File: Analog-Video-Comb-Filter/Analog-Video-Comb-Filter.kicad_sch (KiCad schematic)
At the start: 97 parts, among them J1 12VDC(+), J2 SVHS, J3 CVBS, Q1 BC548, Q10 BC548, Q2 BC548, Q3 BC558, Q4 BC558, Q5 BC548, Q6 BC548, Q7 BC548, Q8 BC558, Q9 BC548, U1 L7805, U2 SAA4961, U3 MC44144, U4 74HC04, U5 LM1881, Y1 See table

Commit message: Replaced RCA connector footprint, added gerber files, fixed README
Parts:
- removed J3: CVBS, Custom_Footprints:RCA_Dual_Switch, symbol Connector:Conn_Coaxial_x2_Isolated
- added J3: CV-OUT, Custom_Footprints:Keystone_973, symbol Custom_Symbols:Conn_Coaxial_Switch
- added J4: CV-IN, Custom_Footprints:Keystone_973, symbol Custom_Symbols:Conn_Coaxial_Switch
- J2: symbol Custom_Symbols:Mini-DIN-4-Shield -> Custom_Symbols:Mini-DIN-4-Gound
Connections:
- net CVBS-IN: now also J4.1 (In)
- net CVBS-OUT: now also J3.1 (In)
- net GND: now also J2.5, J3.2 (Ext), J4.2 (Ext); no longer J2.S
- no-connect marks 12 -> 14
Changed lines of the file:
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@@
   )
   (no_connect (at 278.13 88.9))
+  (no_connect (at 259.08 148.59))
   (no_connect (at 256.54 58.42))
   (no_connect (at 256.54 66.04))
@@
   (no_connect (at 278.13 76.2))
   (no_connect (at 182.88 140.97))
+  (no_connect (at 50.8 181.61))
   (wire (pts (xy 218.44 115.57) (xy 226.06 115.57))
     (stroke (width 0) (type default))
@@
     (stroke (width 0) (type default))
   )
-  (wire (pts (xy 255.27 146.05) (xy 256.54 146.05))
+  (wire (pts (xy 255.27 146.05) (xy 259.08 146.05))
     (stroke (width 0) (type default))
   )
@@
     (stroke (width 0) (type default))
   )
-  (wire (pts (xy 261.62 151.13) (xy 261.62 157.48))
+  (wire (pts (xy 264.16 151.13) (xy 264.16 157.48))
     (stroke (width 0) (type default))
   )
@@
     )
   )
-  (symbol (lib_id "Custom_Symbols:Mini-DIN-4-Shield") (at 45.72 148.59 0) (unit 1)
+  (symbol (lib_id "Custom_Symbols:Mini-DIN-4-Gound") (at 45.72 148.59 0) (unit 1)
     (in_bom yes) (on_board yes) (dnp no)
     (property "Reference" "J2" (at 45.72 139.7 0)
@@
     (pin "3")
     (pin "4")
-    (pin "S")
+    (pin "5")
     (instances
       (project "Analog-Video-Comb-Filter"
@@
     )
   )
-  (symbol (lib_id "Connector:Conn_Coaxial_x2_Isolated") (at 261.62 146.05 0) (unit 1)
+  (symbol (lib_id "Device:C") (at 208.28 99.06 0) (unit 1)
     (in_bom yes) (on_board yes) (dnp no)
-    (property "Reference" "J3" (at 264.16 144.78 0)
+    (property "Reference" "C22" (at 210.82 97.79 0)
       (effects (font (size 1.27 1.27)) (justify left))
     )
-    (property "Value" "CVBS" (at 264.16 147.32 0)
+    (property "Value" "100nF" (at 210.82 100.33 0)
       (effects (font (size 1.27 1.27)) (justify left))
     )
-    (property "Footprint" "Custom_Footprints:RCA_Dual_Switch" (at 261.62 146.05 0)
+    (property "Footprint" "Capacitor_THT:C_Disc_D5.0mm_W2.5mm_P2.50mm" (at 209.2452 102.87 0)
       (effects (font (size 1.27 1.27)) hide)
     )
-    (property "Datasheet" " ~" (at 261.62 146.05 0)
+    (property "Datasheet" "~" (at 208.28 99.06 0)
       (effects (font (size 1.27 1.27)) hide)
     )
     (pin "1")
     (pin "2")
-    (pin "3")
-    (pin "4")
     (instances
       (project "Analog-Video-Comb-Filter"
         (path "/6f7fa11e-654f-4988-a085-8bac964d6c7d"
-          (reference "J3") (unit 1)
+          (reference "C22") (unit 1)
         )
       )
       (project "SAA4960-PAL-comb-filter-v2"
         (path "/ab1269c0-a0e4-4465-9741-f0093d972d6c"
-          (reference "J3") (unit 1)
+          (reference "C22") (unit 1)
         )
       )
     )
   )
-  (symbol (lib_id "Device:C") (at 208.28 99.06 0) (unit 1)
+  (symbol (lib_id "Custom_Symbols:Conn_Coaxial_Switch") (at 45.72 179.07 0) (mirror y) (unit 1)
     (in_bom yes) (on_board yes) (dnp no)
-    (property "Reference" "C22" (at 210.82 97.79 0)
-      (effects (font (size 1.27 1.27)) (justify left))
+    (property "Reference" "J3" (at 46.0374 172.72 0)
+      (effects (font (size 1.27 1.27)))
     )
-    (property "Value" "100nF" (at 210.82 100.33 0)
-      (effects (font (size 1.27 1.27)) (justify left))
+    (property "Value" "CV-OUT" (at 46.0374 175.26 0)
+      (effects (font (size 1.27 1.27)))
     )
-    (property "Footprint" "Capacitor_THT:C_Disc_D5.0mm_W2.5mm_P2.50mm" (at 209.2452 102.87 0)
+    (property "Footprint" "Custom_Footprints:Keystone_973" (at 45.72 179.07 0)
       (effects (font (size 1.27 1.27)) hide)
     )
-    (property "Datasheet" "~" (at 208.28 99.06 0)
+    (property "Datasheet" " ~" (at 45.72 179.07 0)
       (effects (font (size 1.27 1.27)) hide)
     )
     (pin "1")
     (pin "2")
+    (pin "3")
     (instances
       (project "Analog-Video-Comb-Filter"
         (path "/6f7fa11e-654f-4988-a085-8bac964d6c7d"
-          (reference "C22") (unit 1)
-        )
-      )
-      (project "SAA4960-PAL-comb-filter-v2"
-        (path "/ab1269c0-a0e4-4465-9741-f0093d972d6c"
-          (reference "C22") (unit 1)
+          (reference "J3") (unit 1)
         )
       )
@@
     )
   )
-  (symbol (lib_id "Connector:Conn_Coaxial_x2_Isolated") (at 45.72 179.07 0) (mirror y) (unit 2)
-    (in_bom yes) (on_board yes) (dnp no)
-    (property "Reference" "J3" (at 46.0374 172.72 0)
-      (effects (font (size 1.27 1.27)))
-    )
-    (property "Value" "CVBS" (at 46.0374 175.26 0)
-      (effects (font (size 1.27 1.27)))
-    )
-    (property "Footprint" "Custom_Footprints:RCA_Dual_Switch" (at 45.72 179.07 0)
-      (effects (font (size 1.27 1.27)) hide)
-    )
-    (property "Datasheet" " ~" (at 45.72 179.07 0)
-      (effects (font (size 1.27 1.27)) hide)
-    )
-    (pin "1")
-    (pin "2")
-    (pin "3")
-    (pin "4")
-    (instances
-      (project "Analog-Video-Comb-Filter"
-        (path "/6f7fa11e-654f-4988-a085-8bac964d6c7d"
-          (reference "J3") (unit 2)
-        )
-      )
-      (project "SAA4960-PAL-comb-filter-v2"
-        (path "/ab1269c0-a0e4-4465-9741-f0093d972d6c"
-          (reference "J3") (unit 2)
-        )
-      )
-    )
-  )
   (symbol (lib_id "Device:C") (at 146.05 31.75 0) (unit 1)
     (in_bom yes) (on_board yes) (dnp no)
@@
     )
   )
-  (symbol (lib_id "power:GND") (at 261.62 157.48 0) (unit 1)
+  (symbol (lib_id "power:GND") (at 264.16 157.48 0) (unit 1)
     (in_bom yes) (on_board yes) (dnp no)
-    (property "Reference" "#PWR076" (at 261.62 163.83 0)
+    (property "Reference" "#PWR076" (at 264.16 163.83 0)
       (effects (font (size 1.27 1.27)) hide)
     )
-    (property "Value" "GND" (at 261.62 161.29 0)
+    (property "Value" "GND" (at 264.16 161.29 0)
       (effects (font (size 1.27 1.27)))
     )
-    (property "Footprint" "" (at 261.62 157.48 0)
+    (property "Footprint" "" (at 264.16 157.48 0)
       (effects (font (size 1.27 1.27)) hide)
     )
-    (property "Datasheet" "" (at 261.62 157.48 0)
+    (property "Datasheet" "" (at 264.16 157.48 0)
       (effects (font (size 1.27 1.27)) hide)
     )
@@
         )
       )
+    )
+  )
+  (symbol (lib_id "Custom_Symbols:Conn_Coaxial_Switch") (at 264.16 146.05 0) (unit 1)
+    (in_bom yes) (on_board yes) (dnp no)
+    (property "Reference" "J4" (at 263.8426 139.7 0)
+      (effects (font (size 1.27 1.27)))
+    )
+    (property "Value" "CV-IN" (at 263.8426 142.24 0)
+      (effects (font (size 1.27 1.27)))
+    )
+    (property "Footprint" "Custom_Footprints:Keystone_973" (at 264.16 146.05 0)
+      (effects (font (size 1.27 1.27)) hide)
+    )
+    (property "Datasheet" " ~" (at 264.16 146.05 0)
+      (effects (font (size 1.27 1.27)) hide)
+    )
+    (pin "1")
+    (pin "2")
+    (pin "3")
+    (instances
+      (project "Analog-Video-Comb-Filter"
+        (path "/6f7fa11e-654f-4988-a085-8bac964d6c7d"
+          (reference "J4") (unit 1)
+        )
+      )

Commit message: Added alternative footprint for SAA4963
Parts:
- added JP4: CVBYP, Jumper:SolderJumper-2_P1.3mm_Open_RoundedPad1.0x1.5mm, symbol Jumper:SolderJumper_2_Open
- added U6: SAA4963, Package_DIP:DIP-20_W7.62mm_Socket, symbol Custom_Symbols:SAA4963
- U2: value SAA4961 -> SAA4960/61
- renumbered C9 to C10, C15 to C12, C12 to C13, C13 to C14, C17 to C15, C19 to C16, C14 to C17, C21 to C18, C22 to C19, C16 to C20, C24 to C21, C18 to C22, C26 to C23, C29 to C24, C20 to C26, C28 to C27, C30 to C28, C23 to C29, C4 to C3, C32 to C30, C27 to C31, C31 to C32, C5 to C4, C3 to C5, C10 to C7, C7 to C8, C8 to C9
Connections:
- net +5VA: now also U6.4 (VCCA)
- net +5VD: now also U6.15 (VDDD)
- net +5VL: now also U6.18 (VCCPLL)
- net +5VP: now also U6.6 (VCCO)
- net GND: now also U6.16 (DGND), U6.17 (PLLGND), U6.2 (SVHS), U6.5 (AGND), U6.8 (OGND)
- net REFDL: now also U6.10 (REFDL)
- net CVBS: now reaches C27.1, U2.17 (YEXT/CVBS)
- net CVBS: now also JP4.2 (B), U6.13 (CVBS)
- net CSY: now reaches C25.1, U2.19 (CSY)
- net CSY: now also U6.12 (CSY)
- net FSC: now reaches C15.1, U2.1 (FSC)
- net FSC: now also U6.1 (FSC)
- net REFBP: now reaches R26.2, U2.5 (REFBP)
- net REFBP: now also U6.20 (REFBP)
- net DRV-C renamed CO
- net CO: now also U6.9 (CO)
- net DRV-CV renamed CVBSO
- net CVBSO: now also JP4.1 (A)
- net DRV-Y renamed YO
- net YO: now also U6.11 (YO)
- no-connect marks 14 -> 18
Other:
- note added: "SAA4963 alternative Do not use together with SAA4960/61"
- moved on the sheet: C12, C15, C16, C18, C19, C21, C23, C24, C25, C27, C28, C3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

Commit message: Improved PCB layout, readme improvements
- Minimized (unfortunately not eliminated) ground plane interruptions under signal traces.
- Added dedicated location for SAA4963 alternative footprint REFDL filter capacitors. This way they are not far away and the trace to them is not in the way of other traces.
- Better routing of some traces around the SAA4963 alternative footprint.
- More accurate description of PLL tuning method, with pictures.
- Better quality comparison pictures.
- Various other readme fixes.
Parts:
- added C34: 100nF, Capacitor_THT:C_Disc_D5.0mm_W2.5mm_P2.50mm, symbol Device:C
- added C35: 100uF, Capacitor_THT:CP_Radial_D5.0mm_P2.00mm, symbol Device:C_Polarized
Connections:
- net GND: now also C34.2, C35.2
- net REFDL: no longer U6.10 (REFDL)
- new net REFDL_63: C34.1, C35.1, U6.10 (REFDL)
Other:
- moved on the sheet: JP4, U4A, U4C, U4D, U4E, U4F, U6

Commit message: New output amplifier design
The BJT amplifiers have been replaced with high bandwidth rail-to-rail operational amplifiers. This should resolve the issue of the signal becoming malformed when load is connected through a capacitor, and maybe improve the frequency response as well. The old design has been moved to "rev1-bjt-output-amplifier" branch.
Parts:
- removed C3, C4, C7: 1uF, Capacitor_THT:C_Rect_L9.0mm_W4.2mm_P7.50mm_MKT, symbol Device:C
- removed Q1, Q2, Q5, Q6, Q7, Q9: BC548, Package_TO_SOT_THT:TO-92_Inline_Wide, symbol Transistor_BJT:BC548
- removed Q3, Q4, Q8: BC558, Package_TO_SOT_THT:TO-92_Inline_Wide, symbol Transistor_BJT:BC558
- removed R14, R23: 4,7k, Resistor_THT:R_Axial_DIN0207_L6.3mm_D2.5mm_P7.62mm_Horizontal, symbol Device:R
- removed R15, R22, R24: 560R, Resistor_THT:R_Axial_DIN0207_L6.3mm_D2.5mm_P7.62mm_Horizontal, symbol Device:R
- removed R16, R17, R20, R25: 1k, Resistor_THT:R_Axial_DIN0207_L6.3mm_D2.5mm_P7.62mm_Horizontal, symbol Device:R
- removed R18: 75R, Resistor_THT:R_Axial_DIN0207_L6.3mm_D2.5mm_P7.62mm_Horizontal, symbol Device:R
- removed R19: 27R, Resistor_THT:R_Axial_DIN0207_L6.3mm_D2.5mm_P7.62mm_Horizontal, symbol Device:R
- removed R21: 47R, Resistor_THT:R_Axial_DIN0207_L6.3mm_D2.5mm_P7.62mm_Horizontal, symbol Device:R
- added JP1: ALT, Jumper:SolderJumper-2_P1.3mm_Open_RoundedPad1.0x1.5mm, symbol Jumper:SolderJumper_2_Open
- added U2: AD8044, Package_DIP:DIP-14_W7.62mm_Socket, symbol Device:Opamp_Quad
- R10: value 560R -> 10k
- R11, R13: value 560R -> 1k
- R12: value 4,7k -> 10k
- R4: value 27R -> 75R
- R6: value 27R -> 1k
- R8: value 47R -> 10k
- R9: value 47R -> 1k
- renumbered C15 to C10, C13 to C11, C16 to C12, C14 to C13, C18 to C14, C19 to C15, C17 to C16, C21 to C17, C20 to C18, C23 to C19, C24 to C20, C25 to C21, C27 to C23, C28 to C24, C26 to C25, C30 to C26, C29 to C27, C31 to C28, C32 to C29, C5 to C3, C33 to C30, C34 to C31, C35 to C32, C6 to C4, C8 to C5, C9 to C6, C10 to C7, C12 to C8, C11 to C9, JP1 to JP2, JP2 to JP3, JP3 to JP4, JP4 to JP5, Q10 to Q1, R26 to R14, R27 to R15, R28 to R16, R29 to R17, R31 to R18, R30 to R19, R32 to R20, R33 to R21, U2 to U3, U3 to U4, U4 to U5, U5 to U6, U6 to U7
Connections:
- net CVBS-OUT is gone; now on net CVL: J3.1 (In)
- net CVBSO is gone; now on net CVO: JP5.1 (A), U3.15 (CVBSO)
- net +12VA: now also JP1.2 (B), U2.3 (+), U2.4 (V+); no longer R12.2, R4.2, R6.2, R8.2, R9.2
- net CO: now also R8.1, U2.5 (+)
- net GND: now also R10.2, R11.2, R12.2, R13.2, R8.2, R9.2, U2.11 (V-); no longer R13.1, R5.1, R7.1
- net YO: now also R10.1, U2.10 (+)
- net at R6.1: now also R3.2, U2.8
- net at R11.1: now also R6.2, U2.9 (-)
- net at R7.2: now also R13.1, U2.13 (-); no longer R3.2
- net at R2.2: now also R5.1, U2.7; no longer R5.2
- net CVL: now reaches R4.1
- net CVO: now reaches R12.1
- net CVO: now also U2.12 (+)
- net at R9.1: now also R5.2, U2.6 (-)
- net C renamed CL
- net CVBS renamed CV
- net CVBS-IN renamed CV-IN
- net Y renamed YL
- new net: R4.2, R7.1, U2.14
- new net: JP1.1 (A), U2.1, U2.2 (-)
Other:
- moved on the sheet: C10, C12, C14, C15, C17, C19, C20, C21, C23, C24, C26, C31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

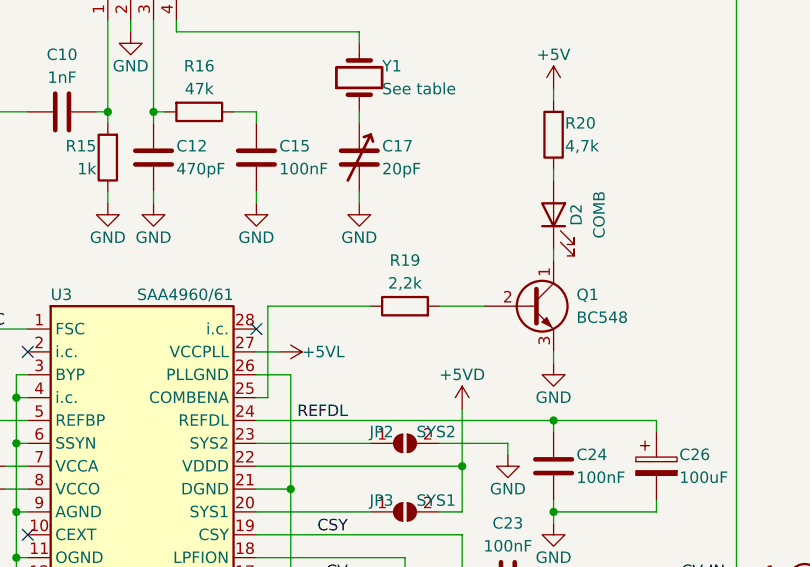
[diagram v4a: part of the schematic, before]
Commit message: Fixed numbering mistakes on PCB, fixed BOM, added color comparison images
- Fixed incorrect R12, R13, R18 and R19 numbers on PCB.
- Removed 560 ohm resistors from parts list.
- Changed 2.2k resistor to 1k as its resistance wasn't critical, now there's one less different part.
- Set solder jumpers and some mutually exclusive parts to be excluded from BOM generation.
- Renamed documentation folder to pdf.
- Added PCB layers in PDF form.
- Added color comparison images, and moved the monochrome comparison images to a collapsible section.
- Added rev.2 assembled PCB photo.
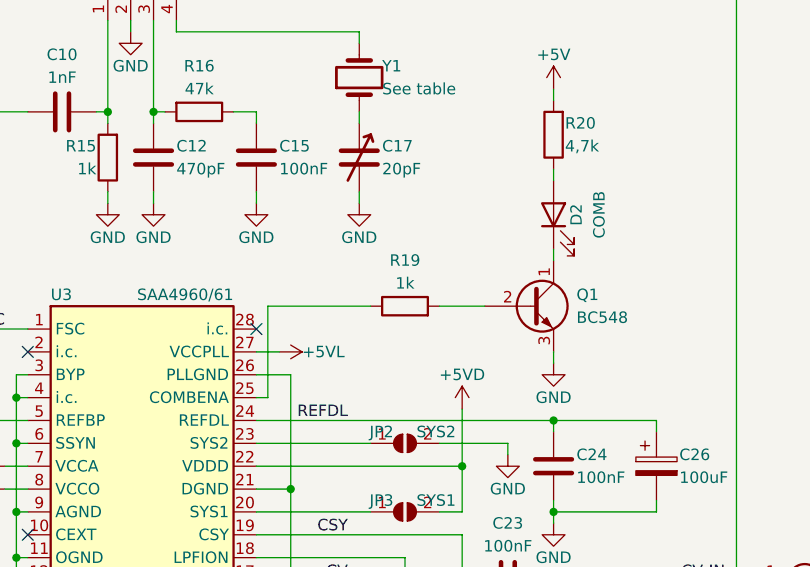
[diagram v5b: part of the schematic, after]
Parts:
- C31, C32, JP1, JP2, JP3, JP4, JP5, U7: now left out of the parts list
- R19: value 2,2k -> 1k
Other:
- title: SAA4960 / SAA4961 Analog Video Comb Filter -> SAA4960 / SAA4961 / SAA4963 Analog Video Comb Filter
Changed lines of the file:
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@@
   (paper "A4")
   (title_block
-    (title "SAA4960 / SAA4961 Analog Video Comb Filter")
-    (date "2026-02-14")
+    (title "SAA4960 / SAA4961 / SAA4963 Analog Video Comb Filter")
+    (date "2026-02-21")
     (rev "2")
     (company "github.com/goscickiw")
@@
   )
   (symbol (lib_id "Device:C_Polarized") (at 267.97 154.94 0) (unit 1)
-    (in_bom yes) (on_board yes) (dnp no)
+    (in_bom no) (on_board yes) (dnp no)
     (property "Reference" "C32" (at 265.43 153.67 0)
       (effects (font (size 1.27 1.27)) (justify right))
@@
   )
   (symbol (lib_id "Jumper:SolderJumper_2_Open") (at 182.88 151.13 270) (unit 1)
-    (in_bom yes) (on_board yes) (dnp no)
+    (in_bom no) (on_board yes) (dnp no)
     (property "Reference" "JP4" (at 181.61 149.86 90)
       (effects (font (size 1.27 1.27)) (justify right))
@@
   )
   (symbol (lib_id "Jumper:SolderJumper_2_Open") (at 182.88 130.81 0) (unit 1)
-    (in_bom yes) (on_board yes) (dnp no)
+    (in_bom no) (on_board yes) (dnp no)
     (property "Reference" "JP2" (at 181.61 129.54 0)
       (effects (font (size 1.27 1.27)) (justify right))
@@
   )
   (symbol (lib_id "Jumper:SolderJumper_2_Open") (at 243.84 151.13 90) (unit 1)
-    (in_bom yes) (on_board yes) (dnp no)
+    (in_bom no) (on_board yes) (dnp no)
     (property "Reference" "JP5" (at 240.03 151.13 0)
       (effects (font (size 1.27 1.27)))
@@
   )
   (symbol (lib_id "Custom_Symbols:SAA4963") (at 260.35 132.08 0) (unit 1)
-    (in_bom yes) (on_board yes) (dnp no) (fields_autoplaced)
+    (in_bom no) (on_board yes) (dnp no) (fields_autoplaced)
     (property "Reference" "U7" (at 252.73 115.57 0) (do_not_autoplace)
       (effects (font (size 1.27 1.27)) (justify left))
@@
   )
   (symbol (lib_id "Jumper:SolderJumper_2_Open") (at 88.9 87.63 0) (unit 1)
-    (in_bom yes) (on_board yes) (dnp no)
+    (in_bom no) (on_board yes) (dnp no)
     (property "Reference" "JP1" (at 88.9 82.55 0)
       (effects (font (size 1.27 1.27)))
@@
   )
   (symbol (lib_id "Jumper:SolderJumper_2_Open") (at 182.88 138.43 0) (unit 1)
-    (in_bom yes) (on_board yes) (dnp no)
+    (in_bom no) (on_board yes) (dnp no)
     (property "Reference" "JP3" (at 181.61 137.16 0)
       (effects (font (size 1.27 1.27)) (justify right))
@@
       (effects (font (size 1.27 1.27)))
     )
-    (property "Value" "2,2k" (at 182.88 113.03 90)
+    (property "Value" "1k" (at 182.88 113.03 90)
       (effects (font (size 1.27 1.27)))
     )
@@
   )
   (symbol (lib_id "Device:C") (at 256.54 154.94 0) (unit 1)
-    (in_bom yes) (on_board yes) (dnp no)
+    (in_bom no) (on_board yes) (dnp no)
     (property "Reference" "C31" (at 254 153.67 0)
       (effects (font (size 1.27 1.27)) (justify right))
